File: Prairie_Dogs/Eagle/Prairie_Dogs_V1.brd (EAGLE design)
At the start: 172.7 x 106.4 mm, 19 parts, among them Q1 MOSFET-NCH, Q2 MOSFET-NCH, U1 ITSYBITSY_5V

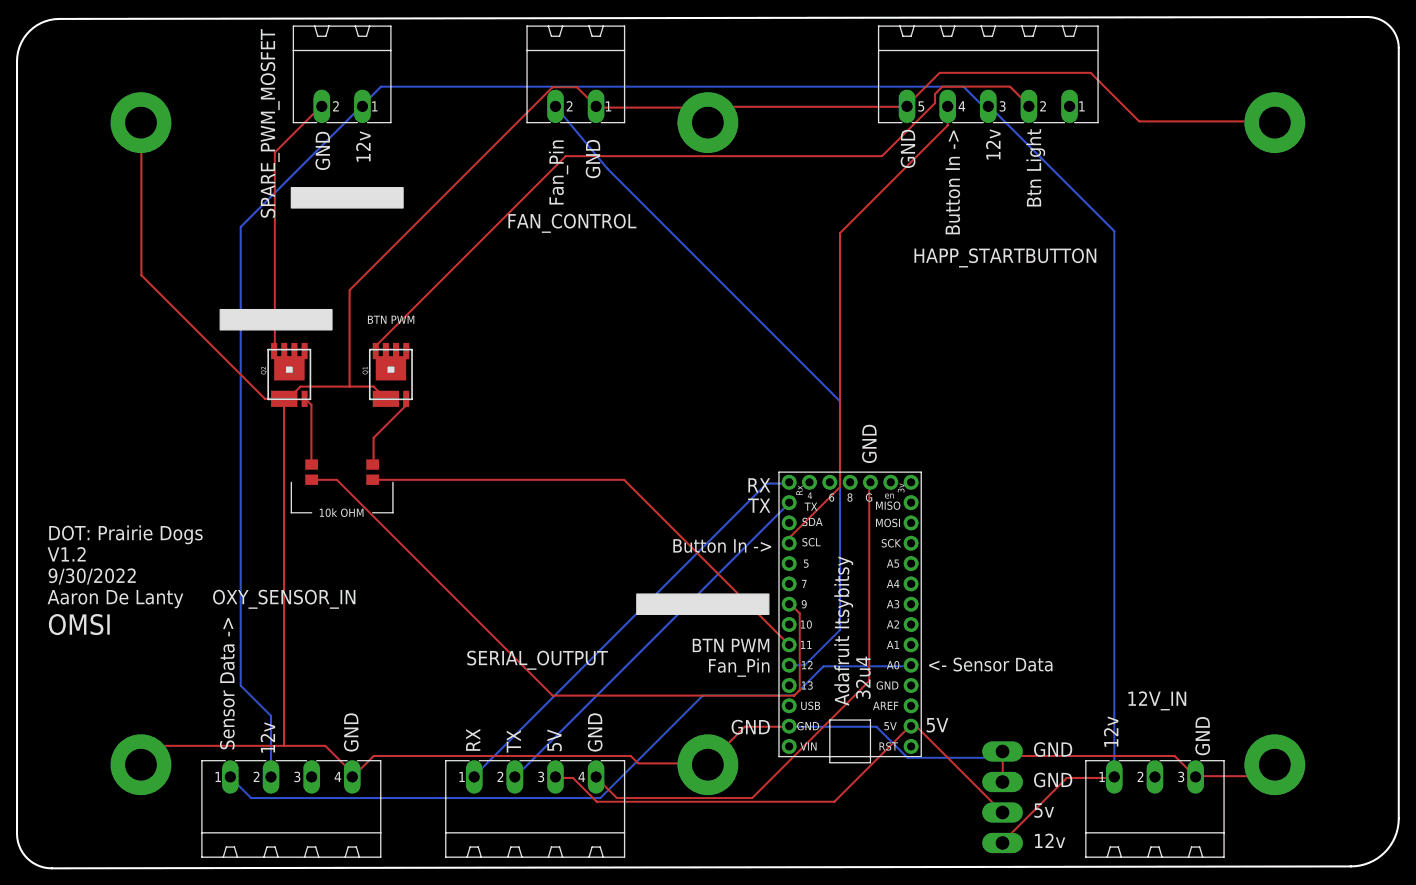
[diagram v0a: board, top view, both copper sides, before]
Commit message: added extra pin to control fan
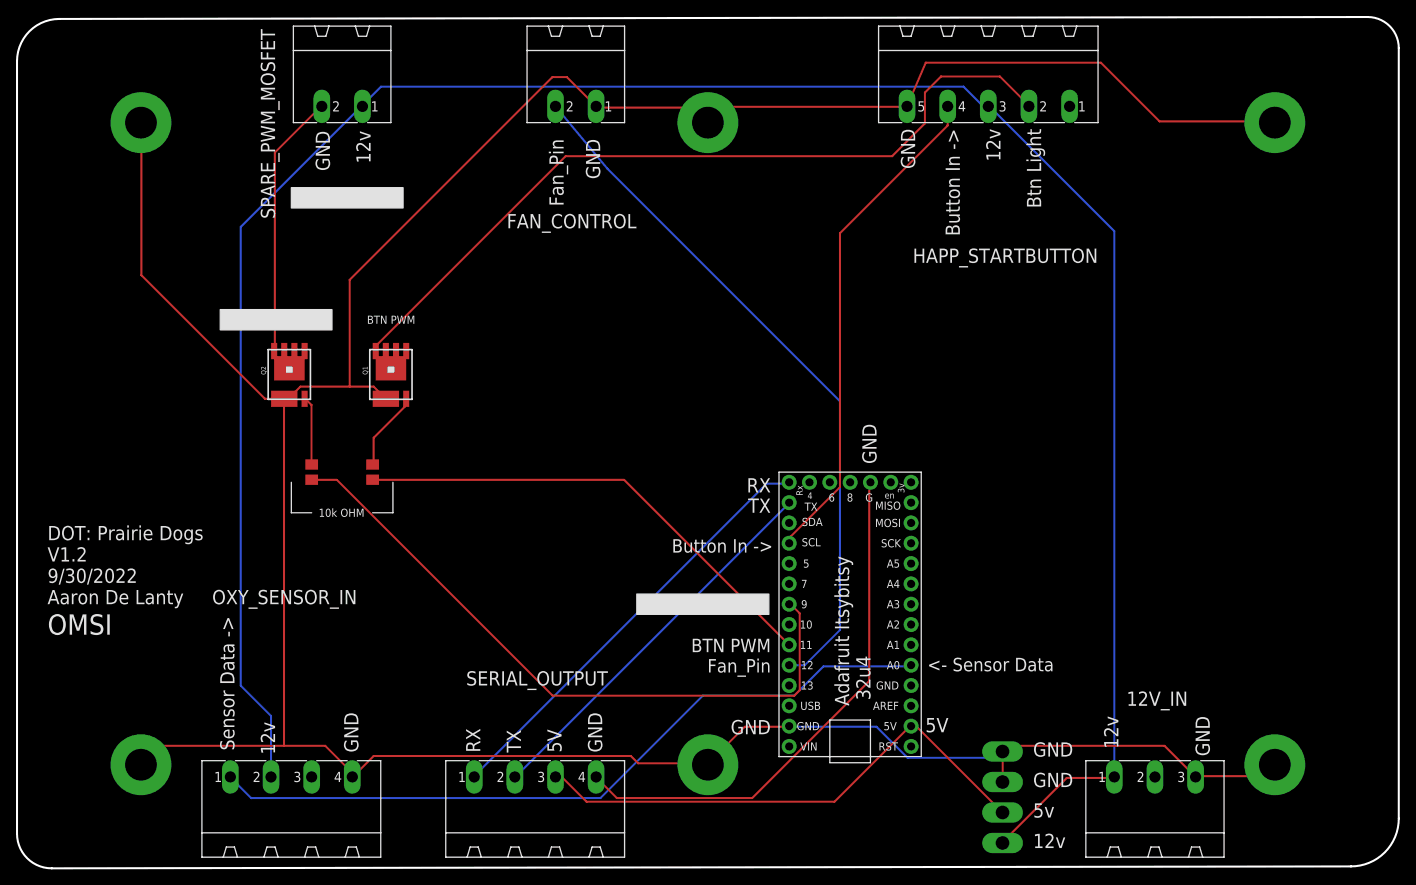
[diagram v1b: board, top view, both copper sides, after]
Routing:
- net GND: track 402.2 -> 407.7 mm
- net N$1: track 97.5 -> 100.1 mm
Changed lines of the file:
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@@
 <attribute name="MF" value="FARNELL" x="53.34" y="7.62" size="1.778" layer="27" display="off"/>
 <attribute name="MPN" value="1757268" x="53.34" y="7.62" size="1.778" layer="27" display="off"/>
-<attribute name="NAME" x="44.704" y="26.67" size="1.778" layer="25" ratio="10"/>
+<attribute name="NAME" x="44.704" y="24.13" size="1.778" layer="25" ratio="10"/>
 <attribute name="OC_FARNELL" value="3705195" x="53.34" y="7.62" size="1.778" layer="27" display="off"/>
 <attribute name="OC_NEWARK" value="71C4163" x="53.34" y="7.62" size="1.778" layer="27" display="off"/>
@@
 <wire x1="99.6696" y1="96.4692" x2="99.822" y2="96.52" width="0.254" layer="1"/>
 <wire x1="74.9808" y1="94.6404" x2="74.93" y2="94.488" width="0.254" layer="1"/>
-<wire x1="128.8542" y1="94.6404" x2="145.6182" y2="94.6404" width="0.254" layer="1"/>
-<wire x1="122.7836" y1="100.711" x2="128.8542" y2="94.6404" width="0.254" layer="1"/>
-<wire x1="103.9114" y1="100.711" x2="122.7836" y2="100.711" width="0.254" layer="1"/>
-<wire x1="99.8982" y1="96.6978" x2="103.9114" y2="100.711" width="0.254" layer="1"/>
+<wire x1="131.3942" y1="94.6404" x2="145.6182" y2="94.6404" width="0.254" layer="1"/>
+<wire x1="124.0536" y1="101.981" x2="131.3942" y2="94.6404" width="0.254" layer="1"/>
+<wire x1="102.16243125" y1="101.981" x2="124.0536" y2="101.981" width="0.254" layer="1"/>
 <wire x1="145.6182" y1="94.6404" x2="145.796" y2="94.488" width="0.254" layer="1"/>
-<wire x1="99.8982" y1="96.6978" x2="99.822" y2="96.52" width="0.254" layer="1"/>
+<wire x1="102.16243125" y1="101.981" x2="99.822" y2="96.52" width="0.254" layer="1"/>
 <wire x1="79.5528" y1="18.9738" x2="85.0392" y2="18.9738" width="0.254" layer="1"/>
 <wire x1="74.9808" y1="14.4018" x2="79.5528" y2="18.9738" width="0.254" layer="1"/>
@@
 <wire x1="74.9808" y1="14.4018" x2="74.93" y2="14.224" width="0.254" layer="1"/>
 <wire x1="111.7854" y1="15.7734" x2="111.7854" y2="15.3162" width="0.254" layer="1"/>
+<wire x1="111.7854" y1="16.5862" x2="111.7854" y2="15.7734" width="0.254" layer="1"/>
 <wire x1="111.7854" y1="15.3162" x2="111.7854" y2="12.1158" width="0.254" layer="1"/>
 <wire x1="111.7854" y1="12.1158" x2="111.76" y2="12.065" width="0.254" layer="1"/>
@@
 <wire x1="136.017" y1="12.8016" x2="135.89" y2="12.7" width="0.254" layer="1"/>
 <wire x1="145.6182" y1="14.1732" x2="145.796" y2="14.224" width="0.254" layer="1"/>
-<wire x1="133.2738" y1="15.3162" x2="111.7854" y2="15.3162" width="0.254" layer="1"/>
-<wire x1="135.7884" y1="12.8016" x2="133.2738" y2="15.3162" width="0.254" layer="1"/>
+<wire x1="132.0038" y1="16.5862" x2="111.7854" y2="16.5862" width="0.254" layer="1"/>
+<wire x1="135.89" y1="12.7" x2="132.0038" y2="16.5862" width="0.254" layer="1"/>
 <wire x1="111.7854" y1="15.3162" x2="111.76" y2="15.875" width="0.254" layer="1"/>
-<wire x1="135.7884" y1="12.8016" x2="135.89" y2="12.7" width="0.254" layer="1"/>
 <wire x1="96.012" y1="18.9738" x2="85.2678" y2="18.9738" width="0.254" layer="16"/>
 <wire x1="99.8982" y1="15.0876" x2="96.012" y2="18.9738" width="0.254" layer="16"/>
@@
 <wire x1="22.6314" y1="60.1218" x2="22.1742" y2="60.1218" width="0.254" layer="1"/>
 <wire x1="24.003" y1="61.4934" x2="22.6314" y2="60.1218" width="0.254" layer="1"/>
-<wire x1="33.147" y1="61.4934" x2="32.6898" y2="61.4934" width="0.254" layer="1"/>
-<wire x1="32.6898" y1="61.4934" x2="30.1498" y2="61.4934" width="0.254" layer="1"/>
+<wire x1="33.147" y1="61.4934" x2="30.1498" y2="61.4934" width="0.254" layer="1"/>
 <wire x1="30.1498" y1="61.4934" x2="24.003" y2="61.4934" width="0.254" layer="1"/>
 <wire x1="34.5186" y1="60.1218" x2="33.147" y2="61.4934" width="0.254" layer="1"/>
@@
 <wire x1="74.7522" y1="14.4018" x2="74.93" y2="14.224" width="0.254" layer="1"/>
 <wire x1="30.6324" y1="12.8016" x2="30.48" y2="12.7" width="0.254" layer="1"/>
-<wire x1="60.96" y1="96.52" x2="58.5724" y2="98.9076" width="0.254" layer="1"/>
-<wire x1="58.5724" y1="98.9076" x2="55.499" y2="98.9076" width="0.254" layer="1"/>
-<wire x1="55.499" y1="98.9076" x2="30.1498" y2="73.5584" width="0.254" layer="1"/>
-<wire x1="30.1498" y1="61.4934" x2="30.1498" y2="73.5584" width="0.254" layer="1"/>
+<wire x1="60.96" y1="96.52" x2="57.3024" y2="100.1776" width="0.254" layer="1"/>
+<wire x1="57.3024" y1="100.1776" x2="55.499" y2="100.1776" width="0.254" layer="1"/>
+<wire x1="55.499" y1="100.1776" x2="30.1498" y2="74.8284" width="0.254" layer="1"/>
+<wire x1="30.1498" y1="61.4934" x2="30.1498" y2="74.8284" width="0.254" layer="1"/>
 </signal>
 <signal name="12V">
@@
 <contactref element="SERIAL_OUTPUT" pad="3"/>
 <wire x1="101.0412" y1="18.9738" x2="100.3554" y2="18.9738" width="0.254" layer="1"/>
-<wire x1="111.5568" y1="8.4582" x2="101.0412" y2="18.9738" width="0.254" layer="1"/>
+<wire x1="111.76" y1="8.255" x2="101.0412" y2="18.9738" width="0.254" layer="1"/>
 <wire x1="100.3554" y1="18.9738" x2="100.33" y2="19.05" width="0.254" layer="1"/>
-<wire x1="111.5568" y1="8.4582" x2="111.76" y2="8.255" width="0.254" layer="1"/>
-<wire x1="58.0644" y1="12.573" x2="56.007" y2="12.573" width="0.254" layer="1"/>
-<wire x1="61.0362" y1="9.6012" x2="58.0644" y2="12.573" width="0.254" layer="1"/>
-<wire x1="90.7542" y1="9.6012" x2="61.0362" y2="9.6012" width="0.254" layer="1"/>
+<wire x1="56.7944" y1="12.573" x2="56.007" y2="12.573" width="0.254" layer="1"/>
+<wire x1="59.7662" y1="9.6012" x2="56.7944" y2="12.573" width="0.254" layer="1"/>
+<wire x1="90.7542" y1="9.6012" x2="59.7662" y2="9.6012" width="0.254" layer="1"/>
 <wire x1="100.1268" y1="18.9738" x2="90.7542" y2="9.6012" width="0.254" layer="1"/>
 <wire x1="56.007" y1="12.573" x2="55.88" y2="12.7" width="0.254" layer="1"/>
@@
 <wire x1="33.6042" y1="66.7512" x2="33.6042" y2="66.0654" width="0.254" layer="1"/>
 <wire x1="57.15" y1="90.297" x2="33.6042" y2="66.7512" width="0.254" layer="1"/>
-<wire x1="96.6978" y1="90.297" x2="57.15" y2="90.297" width="0.254" layer="1"/>
-<wire x1="103.3272" y1="96.9264" x2="96.6978" y2="90.297" width="0.254" layer="1"/>
-<wire x1="103.3272" y1="98.0694" x2="103.3272" y2="96.9264" width="0.254" layer="1"/>
-<wire x1="104.2416" y1="98.9838" x2="103.3272" y2="98.0694" width="0.254" layer="1"/>
-<wire x1="112.6998" y1="98.9838" x2="104.2416" y2="98.9838" width="0.254" layer="1"/>
-<wire x1="114.9858" y1="96.6978" x2="112.6998" y2="98.9838" width="0.254" layer="1"/>
+<wire x1="97.9678" y1="90.297" x2="57.15" y2="90.297" width="0.254" layer="1"/>
+<wire x1="102.0572" y1="94.3864" x2="97.9678" y2="90.297" width="0.254" layer="1"/>
+<wire x1="111.4298" y1="100.2538" x2="104.0638" y2="100.2538" width="0.254" layer="1"/>
+<wire x1="104.0638" y1="100.2538" x2="102.0572" y2="98.2472" width="0.254" layer="1"/>
+<wire x1="102.0572" y1="98.2472" x2="102.0572" y2="94.3864" width="0.254" layer="1"/>
+<wire x1="114.9858" y1="96.6978" x2="111.4298" y2="100.2538" width="0.254" layer="1"/>
 <wire x1="33.6042" y1="66.0654" x2="33.407" y2="65.937" width="0.254" layer="1"/>
 <wire x1="114.9858" y1="96.6978" x2="115.062" y2="96.52" width="0.254" layer="1"/>

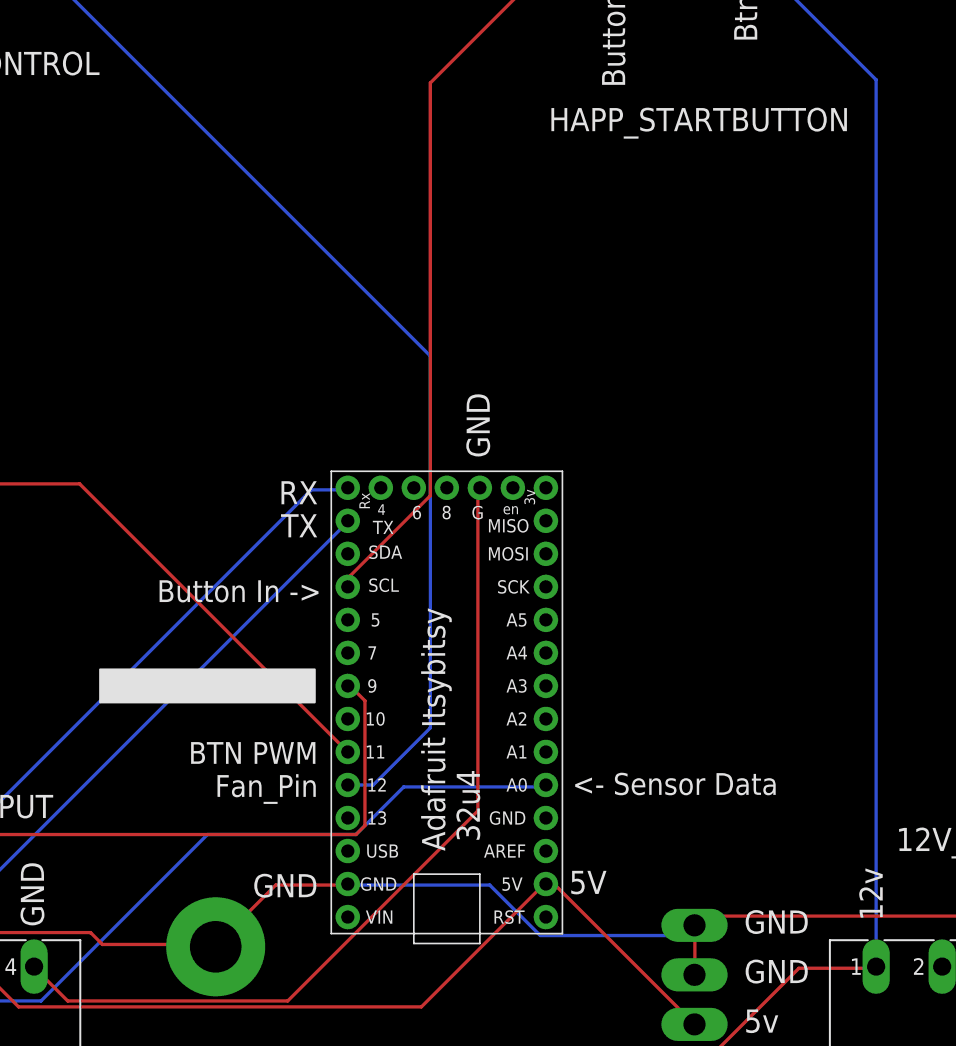
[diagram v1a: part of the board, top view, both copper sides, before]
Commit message: Calibration
Added Calibration routine, current implementation is not production ready. Waiting on new board to add calibration button & to save to EEPROM. This is intended to be ran during first setup at new venues.
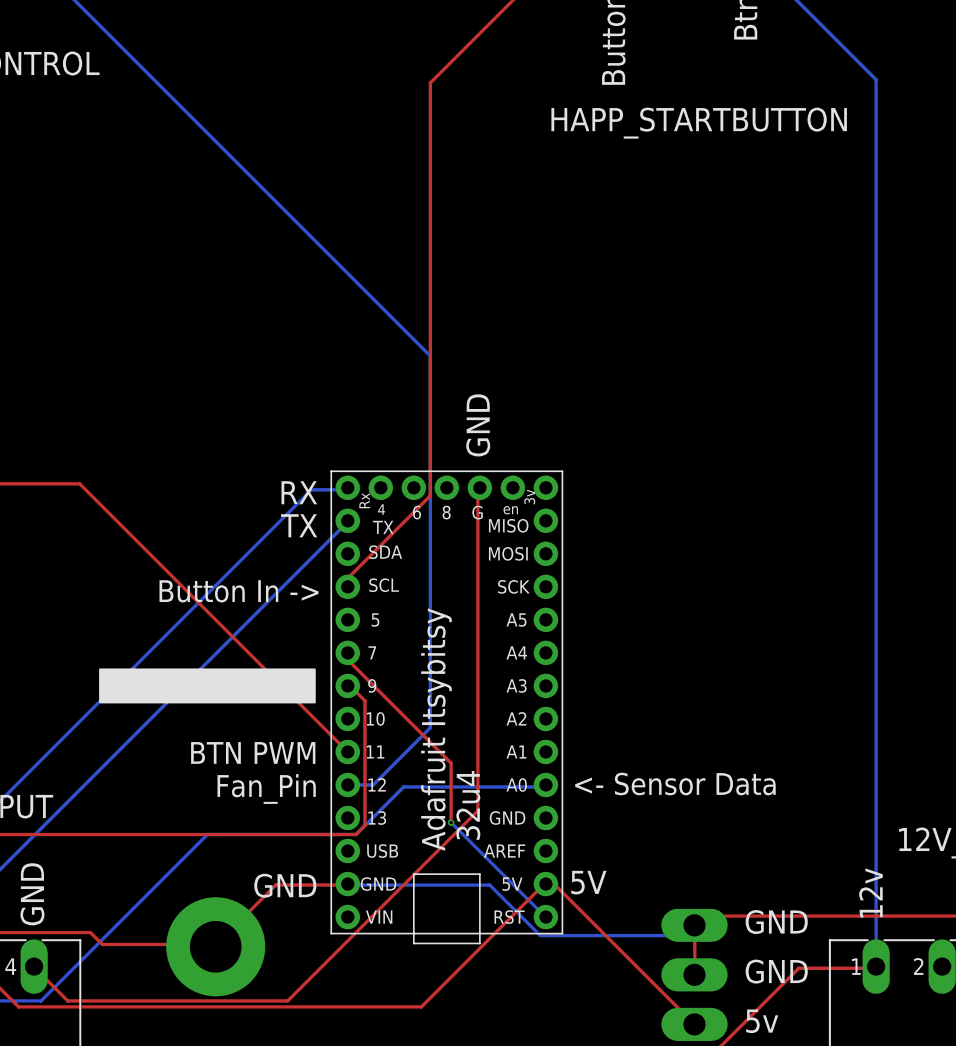
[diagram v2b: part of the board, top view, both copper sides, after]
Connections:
- new net N$13: U1.D7, U1.RES
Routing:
- net N$13: track 0.00 -> 26.7 mm, vias 0 -> 1
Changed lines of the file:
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@@
 <wire x1="109.9566" y1="96.6978" x2="109.982" y2="96.52" width="0.254" layer="16"/>
 <wire x1="31.7754" y1="96.6978" x2="31.75" y2="96.52" width="0.254" layer="16"/>
-<wire x1="125.73" y1="80.9244" x2="125.73" y2="12.8016" width="0.254" layer="16"/>
+<wire x1="125.73" y1="80.9244" x2="125.73" y2="12.7" width="0.254" layer="16"/>
 <wire x1="110.1852" y1="96.4692" x2="125.73" y2="80.9244" width="0.254" layer="16"/>
-<wire x1="125.73" y1="12.8016" x2="125.73" y2="12.7" width="0.254" layer="16"/>
 <wire x1="110.1852" y1="96.4692" x2="109.982" y2="96.52" width="0.254" layer="16"/>
 </signal>
@@
 <contactref element="10K" pad="2"/>
 <wire x1="64.4652" y1="49.8348" x2="33.147" y2="49.8348" width="0.254" layer="1"/>
-<wire x1="85.0392" y1="29.2608" x2="64.4652" y2="49.8348" width="0.254" layer="1"/>
+<wire x1="85.09" y1="29.21" x2="64.4652" y2="49.8348" width="0.254" layer="1"/>
 <wire x1="33.147" y1="49.8348" x2="33.02" y2="49.85" width="0.254" layer="1"/>
-<wire x1="85.0392" y1="29.2608" x2="85.09" y2="29.21" width="0.254" layer="1"/>
 </signal>
 <signal name="N$2">
@@
 <wire x1="62.357" y1="88.7476" x2="55.88" y2="96.52" width="0.254" layer="16"/>
 </signal>
+<signal name="N$13">
+<contactref element="U1" pad="RES"/>
+<contactref element="U1" pad="D7"/>
+<wire x1="85.2678" y1="36.1188" x2="85.2678" y2="36.8046" width="0.254" layer="1"/>
+<wire x1="93.0402" y1="28.3464" x2="85.2678" y2="36.1188" width="0.254" layer="1"/>
+<wire x1="93.0402" y1="23.7744" x2="93.0402" y2="28.3464" width="0.254" layer="1"/>
+<wire x1="100.1268" y1="16.6878" x2="93.0402" y2="23.7744" width="0.254" layer="16"/>
+<wire x1="85.2678" y1="36.8046" x2="85.09" y2="36.83" width="0.254" layer="1"/>
+<wire x1="100.1268" y1="16.6878" x2="100.33" y2="16.51" width="0.254" layer="16"/>
+<via x="93.0402" y="23.7744" extent="1-16" drill="0.254"/>
+</signal>
 </signals>

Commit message: Documentation
Started Documentation
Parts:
- added CALIBRATION_BTN: MSTBA2, th_libraries:MSTBA2
- moved HAPP_STARTBUTTON 14.0 mm to (96.0, 101.6)
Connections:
- removed net N$13: U1.D7, U1.RES
- new net N$14: CALIBRATION_BTN.2, U1.D5
- net GND: now also CALIBRATION_BTN.1
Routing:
- net GND: track 407.7 -> 0.00 mm
- net 12V: track 280.1 -> 0.00 mm
- net N$1: track 100.1 -> 0.00 mm
- net N$3: track 93.1 -> 0.00 mm
- net N$12: track 88.0 -> 0.00 mm
- net N$5: track 83.9 -> 0.00 mm
- net N$10: track 66.2 -> 0.00 mm
- net 5V: track 65.6 -> 0.00 mm
- net N$2: track 62.8 -> 0.00 mm
- net N$9: track 60.6 -> 0.00 mm
- net N$11: track 54.7 -> 0.00 mm
- net N$8: track 48.5 -> 0.00 mm
- net N$4: track 33.1 -> 0.00 mm
- net N$13: track 26.7 -> 0.00 mm, vias 1 -> 0
- net N$6: track 10.00 -> 0.00 mm
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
